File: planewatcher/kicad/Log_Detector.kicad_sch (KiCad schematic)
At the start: 17 parts, among them U9 ADL5513

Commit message: fix R43 metadata
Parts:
- R43: Notes Series resistor in tunable 50 ohm attenuator "pi pad" footp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 -> (none); Purpose Zero-ohm link tying ADL5513 VOUT to VSET for measurement mo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 -> Series resistor in tunable 50 ohm attenuator "pi pad" footp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
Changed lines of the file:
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@@
 			)
 		)
-		(property "Purpose" "Zero-ohm link tying ADL5513 VOUT to VSET for measurement mode."
+		(property "Purpose" "Series resistor in tunable 50 ohm attenuator \"pi pad\" footprint."
 			(at 59.69 62.23 0)
 			(hide yes)
 			(show_name no)
-			(do_not_autoplace no)
-			(effects
-				(font
-					(size 1.27 1.27)
-				)
-			)
-		)
-		(property "Notes" "Series resistor in tunable 50 ohm attenuator \"pi pad\" footprint."
-			(at 59.69 62.23 90)
-			(hide yes)
-			(show_name no)

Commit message: Add persistent PCBWay BOM fields to KiCad schematic
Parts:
- C40, C44: MPN (none) -> GRM155R71H104KE14D; Manufacturer (none) -> Murata; Package (none) -> 0402
- C41, C45: MPN (none) -> GRM1555C1H101JA01D; Manufacturer (none) -> Murata; Package (none) -> 0402
- C42, C43: MPN (none) -> GRM155R71H473KE14D; Manufacturer (none) -> Murata; Package (none) -> 0402
- C70: MPN (none) -> GRM155R71H103KA88D; Manufacturer (none) -> Murata; Package (none) -> 0402
- R25: MPN (none) -> ERA-2AEB52R3X; Manufacturer (none) -> Panasonic; Package (none) -> 0402
- R26: MPN (none) -> ERA-2AEB4992X; Manufacturer (none) -> Panasonic; Package (none) -> 0402
- R27: MPN (none) -> ERA-2AEB9531X; Manufacturer (none) -> Panasonic; Package (none) -> 0402
- R41, R42: MPN (none) -> CRCW0402 (TBD); Manufacturer (none) -> Vishay; Package (none) -> 0402
- R43: MPN (none) -> RC0402JR-070RL; Manufacturer (none) -> Yageo; Package (none) -> 0402
- RV1: MPN (none) -> 3224W-1-102E; Manufacturer (none) -> Bourns; Package (none) -> 3224W (SMD trim pot)
- U9: MPN (none) -> ADL5513ACPZ-R7; Manufacturer (none) -> Analog Devices; Package (none) -> LFCSP-16 (3x3mm)

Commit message: move power supply and add GPS module
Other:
- title: Plane Watcher: Log Detector Section -> Plane Watcher
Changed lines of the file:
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@@
 	(paper "A4")
 	(title_block
-		(title "Plane Watcher: Log Detector Section")
-		(date "2026-05-16")
-		(rev "prototype 1.1")
+		(title "Plane Watcher")
+		(date "2026-05-18")
+		(rev "prototype 1.2")
 		(company "plane.watch")
 	)

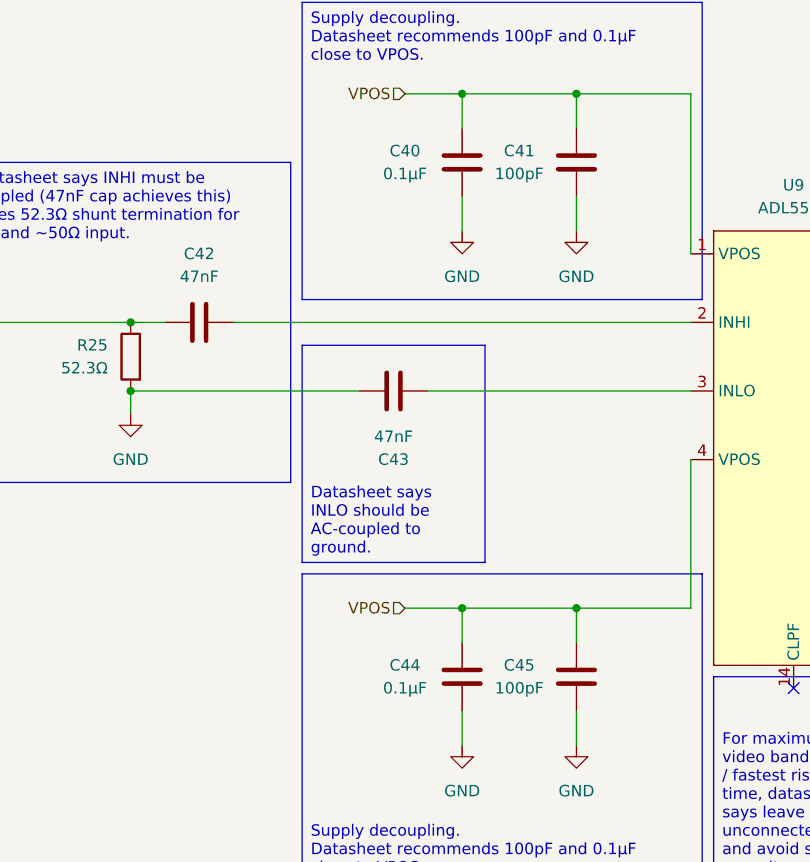
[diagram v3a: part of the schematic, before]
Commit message: review & consolidate all capacitors
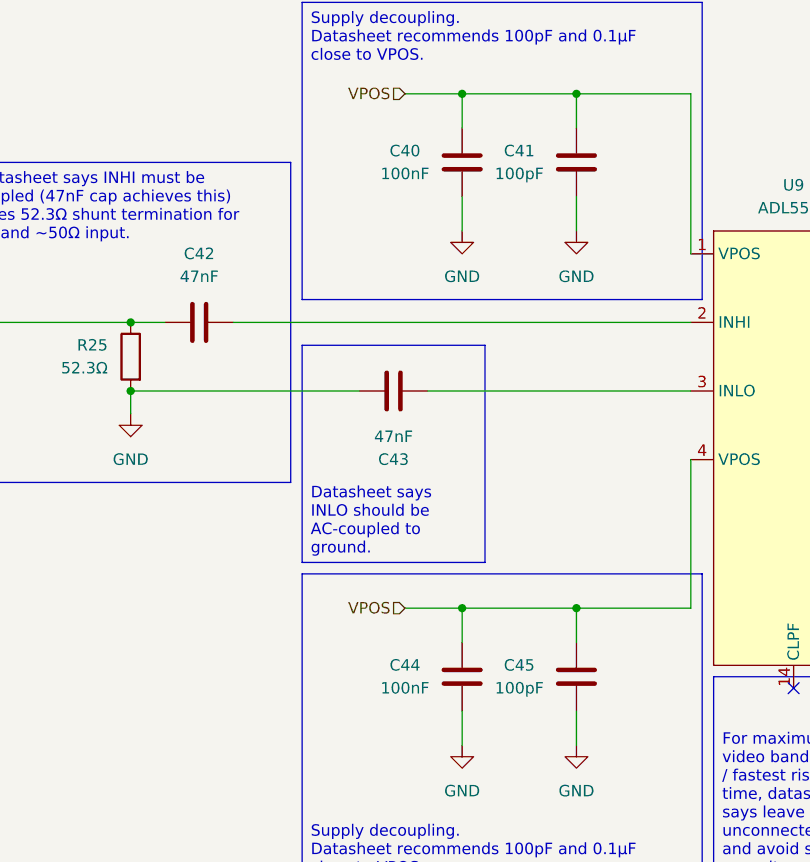
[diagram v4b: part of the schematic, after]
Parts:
- C40, C44: value 0.1µF -> 100nF; MPN GRM155R71H104KE14D -> GCM155R71A104KA55D; Manufacturer Murata -> Murata Electronics; Package 0402 -> 0402 (1005 Metric); Suggested Part Murata GRM155R71H104KE14D -> (none)
- C41, C45: MPN GRM1555C1H101JA01D -> GCM1555C1H101FA16D; Manufacturer Murata -> Murata Electronics; Package 0402 -> 0402 (1005 Metric); Suggested Part Murata GRM1555C1H101JA01D -> (none)
- C42, C43: MPN GRM155R71H473KE14D -> GRM155R71A473KA01D; Manufacturer Murata -> Murata Electronics; Package 0402 -> 0402 (1005 Metric); Suggested Part Murata GRM155R71H473KE14D -> (none)
- C70: MPN GRM155R71H103KA88D -> GRM155R71C103KA01D; Manufacturer Murata -> Murata Electronics; Package 0402 -> 0402 (1005 Metric); Purpose ADL5513 VOUT/VSET measurement-mode support capacitor in the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 -> ADL5513 TADJ decoupling cap.; Suggested Part Murata GRM155R71H103KA88D -> (none)
- R25: Suggested Part Panasonic ERA-2AEB52R3X -> (none)
- R26: Suggested Part ${RTADJ_VPOS_Suggested_Part} -> (none)
- R27: Suggested Part ${RTADJ_GND_Suggested_Part} -> (none)
- R41, R42: Suggested Part DNP by default; fit Vishay CRCW0402 value selected from att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 -> (none)
- R43: Suggested Part Yageo RC0402JR-070RL -> (none)
- RV1: Suggested Part Bourns 3224W-1-102E -> (none)
- TP13, TP14: Suggested Part No fitted part (PCB pad only) -> (none)
- U9: Suggested Part Analog Devices ADL5513ACPZ-R7 -> (none)

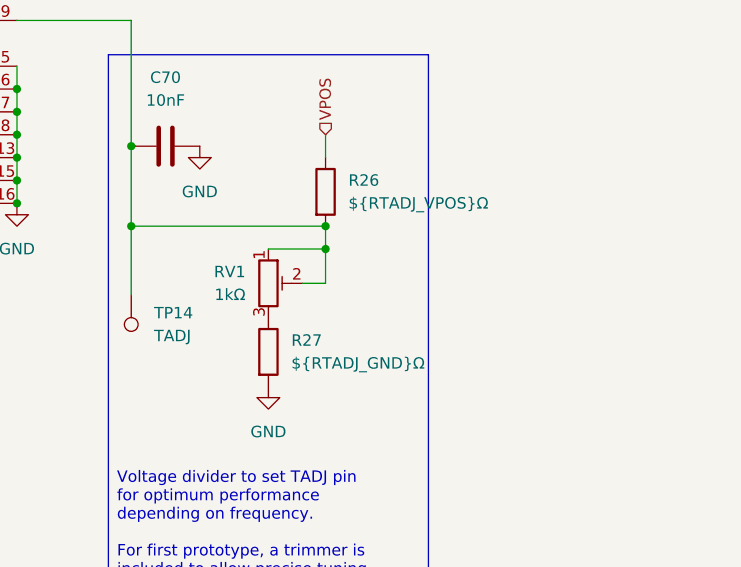
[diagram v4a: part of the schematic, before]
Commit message: review & consolidate all resistors
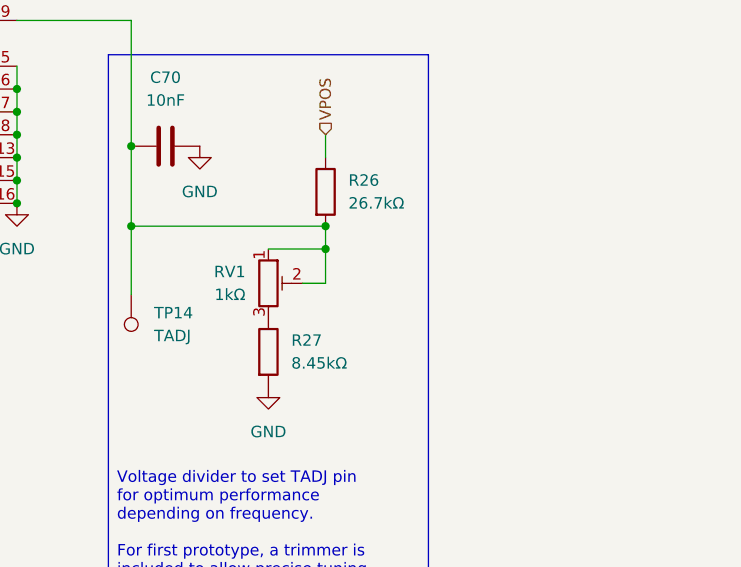
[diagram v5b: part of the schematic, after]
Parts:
- R25: Manufacturer Panasonic -> Panasonic Industry; Package 0402 -> 0402 (1005 Metric)
- R26: value ${RTADJ_VPOS}Ω -> 26.7kΩ; MPN ERA-2AEB4992X -> ERA-2ARB2672X; Manufacturer Panasonic -> Panasonic Industry; Package 0402 -> 0402 (1005 Metric)
- R27: value ${RTADJ_GND}Ω -> 8.45kΩ; MPN ERA-2AEB9531X -> ERA-2ARB8451X; Manufacturer Panasonic -> Panasonic Industry; Package 0402 -> 0402 (1005 Metric)
- R43: MPN RC0402JR-070RL -> ERJ-2GE0R00X; Manufacturer Yageo -> Panasonic Industry; Package 0402 -> 0402 (1005 Metric)
- RV1: Manufacturer Bourns -> Bourns Inc.
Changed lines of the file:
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@@
 			)
 		)
-		(property "Datasheet" ""
+		(property "Datasheet" "https://www.bourns.com/docs/Product-Datasheets/3224.pdf"
 			(at 214.63 106.68 0)
 			(hide yes)
@@
 			)
 		)
-		(property "Description" "1kΩ sealed SMD trim potentiometer, top-adjust, Bourns 3224W footprint"
+		(property "Description" "1 kOhms 0.25W, 1/4W J Lead Surface Mount Trimmer Potentiometer Cermet 12.0 Turn Top Adjustment"
 			(at 214.63 106.68 0)
 			(hide yes)
@@
 			)
 		)
-		(property "Manufacturer" "Bourns"
+		(property "Manufacturer" "Bourns Inc."
 			(at 214.63 106.68 0)
 			(hide yes)
@@
 			)
 		)
-		(property "Datasheet" ""
+		(property "Datasheet" "https://industrial.panasonic.com/ww/products/pt/general-purpose-chip-resistors/models/ERJ2GE0R00X"
 			(at 59.69 62.23 0)
 			(hide yes)
@@
 			)
 		)
-		(property "Description" "0Ω jumper, 0402 chip resistor"
+		(property "Description" "0 Ohms Jumper Chip Resistor 0402 (1005 Metric) Automotive AEC-Q200 Thick Film"
 			(at 59.69 62.23 0)
 			(hide yes)
@@
 			)
 		)
-		(property "Package" "0402"
+		(property "Package" "0402 (1005 Metric)"
 			(at 59.69 62.23 0)
 			(hide yes)
@@
 			)
 		)
-		(property "MPN" "RC0402JR-070RL"
+		(property "MPN" "ERJ-2GE0R00X"
 			(at 59.69 62.23 0)
 			(hide yes)
@@
 			)
 		)
-		(property "Manufacturer" "Yageo"
+		(property "Manufacturer" "Panasonic Industry"
 			(at 59.69 62.23 0)
 			(hide yes)
@@
 			)
 		)
-		(property "Value" "${RTADJ_VPOS}Ω"
+		(property "Value" "26.7kΩ"
 			(at 223.52 97.7899 0)
 			(show_name no)
@@
 			)
 		)
-		(property "Datasheet" ""
+		(property "Datasheet" "https://industrial.panasonic.com/cdbs/www-data/pdf/RDM0000/AOA0000C307.pdf"
 			(at 220.98 96.52 0)
 			(hide yes)
@@
 			)
 		)
-		(property "Description" "${RTADJ_VPOS}Ω, ±0.1%, thin film, ≤25ppm/°C, 0402 chip resistor"
+		(property "Description" "26.7 kOhms ±0.1% 0.063W, 1/16W Chip Resistor 0402 (1005 Metric) Automotive AEC-Q200 Thin Film"
 			(at 220.98 96.52 0)
 			(hide yes)
@@
 			)
 		)
-		(property "Package" "0402"
+		(property "Package" "0402 (1005 Metric) "
 			(at 220.98 96.52 0)
 			(hide yes)
@@
 			)
 		)
-		(property "MPN" "ERA-2AEB4992X"
+		(property "MPN" "ERA-2ARB2672X"
 			(at 220.98 96.52 0)
 			(hide yes)
@@
 			)
 		)
-		(property "Manufacturer" "Panasonic"
+		(property "Manufacturer" "Panasonic Industry"
 			(at 220.98 96.52 0)
 			(hide yes)
@@
 			)
 		)
-		(property "Value" "${RTADJ_GND}Ω"
+		(property "Value" "8.45kΩ"
 			(at 217.17 115.5699 0)
 			(show_name no)
@@
 			)
 		)
-		(property "Datasheet" ""
+		(property "Datasheet" "https://industrial.panasonic.com/cdbs/www-data/pdf/RDM0000/AOA0000C307.pdf"
 			(at 214.63 114.3 0)
 			(hide yes)
@@
 			)
 		)
-		(property "Description" "${RTADJ_GND}Ω, ±0.1%, thin film, ≤25ppm/°C, 0402 chip resistor"
+		(property "Description" "8.45 kOhms ±0.1% 0.063W, 1/16W Chip Resistor 0402 (1005 Metric) Automotive AEC-Q200 Thin Film"
 			(at 214.63 114.3 0)
 			(hide yes)
@@
 			)
 		)
-		(property "Package" "0402"
+		(property "Package" "0402 (1005 Metric)"
 			(at 214.63 114.3 0)
 			(hide yes)
@@
 			)
 		)
-		(property "MPN" "ERA-2AEB9531X"
+		(property "MPN" "ERA-2ARB8451X"
 			(at 214.63 114.3 0)
 			(hide yes)
@@
 			)
 		)
-		(property "Manufacturer" "Panasonic"
+		(property "Manufacturer" "Panasonic Industry"
 			(at 214.63 114.3 0)
 			(hide yes)
@@
 			)
 		)
-		(property "Datasheet" ""
+		(property "Datasheet" "https://industrial.panasonic.com/cdbs/www-data/pdf/RDM0000/AOA0000C307.pdf"
 			(at 101.6 66.04 0)
 			(hide yes)
@@
 			)
 		)
-		(property "Description" "52.3Ω, ±0.1%, thin film, ≤25ppm/°C, 0402 chip resistor"
+		(property "Description" "52.3 Ohms ±0.1% 0.063W, 1/16W Chip Resistor 0402 (1005 Metric) Automotive AEC-Q200 Thin Film"
 			(at 101.6 66.04 0)
 			(hide yes)
@@
 			)
 		)
-		(property "Package" "0402"
+		(property "Package" "0402 (1005 Metric)"
 			(at 101.6 66.04 0)
 			(hide yes)
@@
 			)
 		)
-		(property "Manufacturer" "Panasonic"
+		(property "Manufacturer" "Panasonic Industry"
 			(at 101.6 66.04 0)
 			(hide yes)

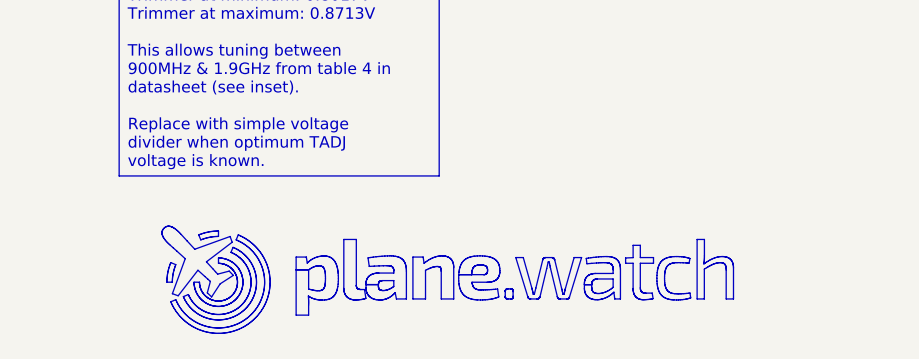
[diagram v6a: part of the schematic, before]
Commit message: add license & copyright info to schematic and pcb. fix layer window.
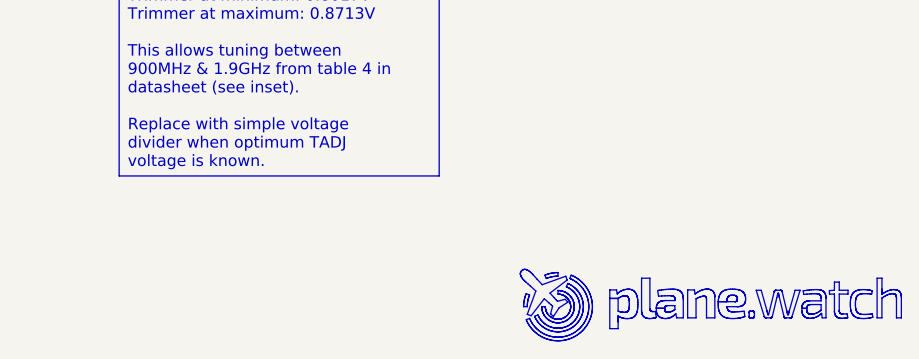
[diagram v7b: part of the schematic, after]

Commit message: added lcsc_ids to all parts
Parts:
- C40, C44: lcsc_id (none) -> C161163
- C41, C45: lcsc_id (none) -> C2941926
- C42, C43: lcsc_id (none) -> C113049
- C70: lcsc_id (none) -> C85735
- R25: lcsc_id (none) -> C2088289
- R26: lcsc_id (none) -> C4221522
- R27: lcsc_id (none) -> C4151733
- R43: lcsc_id (none) -> C242160
- RV1: lcsc_id (none) -> C50204
- U9: lcsc_id (none) -> C579160
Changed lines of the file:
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@@
+			)
+		)
+		(property "lcsc_id" "C50204"
+			(at 214.63 106.68 0)
+			(hide yes)
+			(show_name no)
+			(do_not_autoplace no)
+			(effects
+				(font
+					(size 1.27 1.27)
+				)
 			)
 		)
@@
 			)
 		)
+		(property "lcsc_id" "C161163"
+			(at 138.43 44.45 0)
+			(hide yes)
+			(show_name no)
+			(do_not_autoplace no)
+			(effects
+				(font
+					(size 1.27 1.27)
+				)
+			)
+		)
 		(pin "1"
 		)
@@
 		(property "Notes" ""
 			(at 151.13 44.45 90)
+			(hide yes)
+			(show_name no)
+			(do_not_autoplace no)
+			(effects
+				(font
+					(size 1.27 1.27)
+				)
+			)
+		)
+		(property "lcsc_id" "C2941926"
+			(at 151.13 44.45 0)
 			(hide yes)
 			(show_name no)
@@
 			)
 		)
+		(property "lcsc_id" "C113049"
+			(at 130.81 69.85 0)
+			(hide yes)
+			(show_name no)
+			(do_not_autoplace no)
+			(effects
+				(font
+					(size 1.27 1.27)
+				)
+			)
+		)
 		(pin "1"
 		)
@@
 		(property "Notes" ""
 			(at 151.13 101.6 90)
+			(hide yes)
+			(show_name no)
+			(do_not_autoplace no)
+			(effects
+				(font
+					(size 1.27 1.27)
+				)
+			)
+		)
+		(property "lcsc_id" "C2941926"
+			(at 151.13 101.6 0)
 			(hide yes)
 			(show_name no)
@@
 			)
 		)
+		(property "lcsc_id" "C579160"
+			(at 175.26 50.8 0)
+			(hide yes)
+			(show_name no)
+			(do_not_autoplace no)
+			(effects
+				(font
+					(size 1.27 1.27)
+				)
+			)
+		)
 		(pin "3"
 		)
@@
 			)
 		)
+		(property "lcsc_id" "C85735"
+			(at 203.2 91.44 0)
+			(hide yes)
+			(show_name no)
+			(do_not_autoplace no)
+			(effects
+				(font
+					(size 1.27 1.27)
+				)
+			)
+		)
 		(pin "2"
 		)
@@
 			)
 		)
+		(property "lcsc_id" "C242160"
+			(at 59.69 62.23 0)
+			(hide yes)
+			(show_name no)
+			(do_not_autoplace no)
+			(effects
+				(font
+					(size 1.27 1.27)
+				)
+			)
+		)
 		(pin "1"
 		)
@@
 		(property "Notes" ""
 			(at 138.43 101.6 90)
+			(hide yes)
+			(show_name no)
+			(do_not_autoplace no)
+			(effects
+				(font
+					(size 1.27 1.27)
+				)
+			)
+		)
+		(property "lcsc_id" "C161163"
+			(at 138.43 101.6 0)
 			(hide yes)
 			(show_name no)
@@
 			)
 		)
+		(property "lcsc_id" "C113049"
+			(at 109.22 62.23 0)
+			(hide yes)
+			(show_name no)
+			(do_not_autoplace no)
+			(effects
+				(font
+					(size 1.27 1.27)
+				)
+			)
+		)
 		(pin "2"
 		)
@@
 			)
 		)
+		(property "lcsc_id" "C4221522"
+			(at 220.98 96.52 0)
+			(hide yes)
+			(show_name no)
+			(do_not_autoplace no)
+			(effects
+				(font
+					(size 1.27 1.27)
+				)
+			)
+		)
 		(pin "2"
 		)
@@
 			)
 		)
+		(property "lcsc_id" "C4151733"
+			(at 214.63 114.3 0)
+			(hide yes)
+			(show_name no)
+			(do_not_autoplace no)
+			(effects
+				(font
+					(size 1.27 1.27)
+				)
+			)
+		)
 		(pin "2"
 		)
@@
 			(at 101.6 66.04 0)
 			(hide yes)
+			(show_name no)
+			(do_not_autoplace no)
+			(effects
+				(font
+					(size 1.27 1.27)
+				)
+			)
+		)
+		(property "lcsc_id" "C2088289"
+			(at 101.6 66.04 0)
+			(hide yes)
